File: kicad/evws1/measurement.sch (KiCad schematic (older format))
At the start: 0 parts

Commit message: ...
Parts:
- added C40: 100n, Project:c-1206-hand-soldering, symbol Device:C_Small
- added C41, C42, C43, C44: 10n, Project:c-1206-hand-soldering, symbol Device:C_Small
- added C45, C46: 1n, Project:c-1206-hand-soldering, symbol Device:C_Small
- added R59, R60: 100R, Project:r-0805-hand-soldering, symbol Device:R
- added R81, R82: 820R, Project:r-0805-hand-soldering, symbol Device:R
- added R83, R84: 1K2, Project:r-0805-hand-soldering, symbol Device:R
- added R85, R87: 18K, Project:r-0805-hand-soldering, symbol Device:R
- added R86, R88: 0R, Project:r-0805-hand-soldering, symbol Device:R
- added R89, R90: 15K, Project:r-0805-hand-soldering, symbol Device:R
- added RV2, RV3: 100R, Project:trimmer-tht-3296, symbol Device:R_POT_TRIM
- added RV4, RV5, RV6, RV7: 1K, Project:trimmer-tht-3296, symbol Device:R_POT_TRIM
- added U13: LM224, Project:soic-16_hand-soldering, symbol _project:LM224
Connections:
- net AD-I1: now also C45.2, RV6.2
- net AD-I2: now also C46.2, RV7.2
- net AD-V1: now also C43.2, R89.1, U13.7
- net AD-V2: now also C44.2, R90.1, U13.14
- net I1: now also RV6.1
- net I2: now also RV7.1
- net V1P: now also R59.2
- net V2P: now also R60.2
- net VREF-2V5: now also RV4.3, RV5.3
- new net: C41.1, R59.1, R81.2, U13.2 (-)
- new net: C41.2, R83.2, RV2.1, RV2.2, U13.1
- new net: C43.1, R83.1, R86.1, R89.2, U13.6 (-)
- new net: R81.1, RV2.3
- new net: R85.2, RV4.1, RV4.2
- new net: R85.1, R86.2
- new net: C42.1, R60.1, R82.2, U13.9 (-)
- new net: C42.2, R84.2, RV3.1, RV3.2, U13.8
- new net: C44.1, R84.1, R88.1, R90.2, U13.13 (-)
- new net: R82.1, RV3.3
- new net: R87.2, RV5.1, RV5.2
- new net: R87.1, R88.2
- new net +12V: C40.2, U13.4 (V+)
- new net -12V: U13.11 (V-)
- new net GND: C40.1, C45.1, C46.1, RV6.3, RV7.3, U13.10 (+), U13.12 (+), U13.3 (+), U13.5 (+)
- no-connect marks 0 -> 1

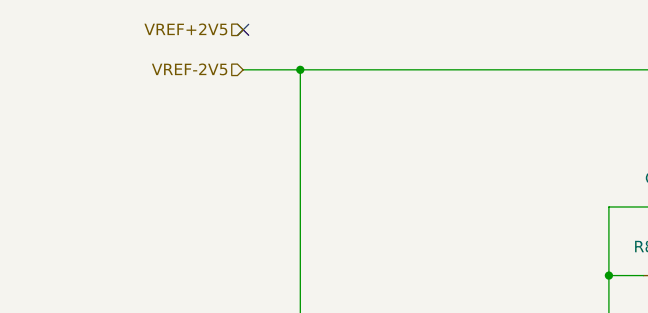
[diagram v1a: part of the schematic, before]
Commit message: Schematic completed, no DRC errors left
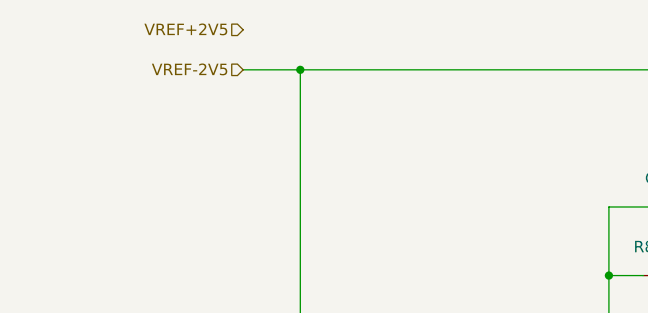
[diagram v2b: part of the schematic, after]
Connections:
- no-connect marks 1 -> 0
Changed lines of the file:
@@
 Text HLabel 2050 925  0    50   Input ~ 0
 VREF+2V5
-NoConn ~ 2050 925
 $Comp
 L power:GND #PWR?

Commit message: schematic finished
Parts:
- added D18, D19: BAT54S, Project:sot-23_hand-soldering, symbol _project:BAT54S
- added J21, J22: header, Project:idc-header-1x03-p2.54mm-vertical, symbol Connector_Generic:Conn_01x03
- added R6, R7: 1K, Project:r-0805-hand-soldering, symbol Device:R
- R83, R84: value 1K2 -> 3K3
- R85, R87: value 18K -> 15K
- R86, R88: value 0R -> 4K7
- R89, R90: value 15K -> 10K
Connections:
- net AD-I1: now also J21.3 (Pin_3)
- net AD-I2: now also J22.3 (Pin_3)
- net AD-V1: now also D18.3, J21.2 (Pin_2), R6.1; no longer C43.2, R89.1, U13.7
- net AD-V2: now also D19.3, J22.2 (Pin_2), R7.1; no longer C44.2, R90.1, U13.14
- net GND: now also D18.1, D19.1, J21.1 (Pin_1), J22.1 (Pin_1)
- new net: C43.2, R6.2, R89.1, U13.7
- new net: C44.2, R7.2, R90.1, U13.14
- new net +5V: D18.2, D19.2
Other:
- moved on the sheet: C42, C44, C45, C46, R60, R82, R83, R84, R87, R88, R90, RV3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

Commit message: ...
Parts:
- removed U13: LM224, Project:soic-16_hand-soldering, symbol _project:LM224
- added C52, C53, C54: 100n, Project:c-1206-hand-soldering, symbol Device:C_Small
- added U13, U14: LM258, Project:soic-8_hand-soldering, symbol _project:LM258
- R59, R6, R60, R7, R81, R82, R83, R84, R85, R86, R87, R88, R89, R90: footprint Project:r-0805-hand-soldering -> Project:r-1206-hand-soldering
- renumbered RV4 to RV3, RV3 to RV4
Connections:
- net +12V: now also C52.2, U13.4 (V-), U14.4 (V-)
- net -12V: now also C53.1, C54.1, U13.8 (V+), U14.8 (V+)
- net GND: now also C52.1, C53.2, C54.2, U13.3 (+), U13.5 (+), U14.3 (+), U14.5 (+)
- net at C41.1, R59.1, R81.2: now also U13.2 (-)
- net at C41.2, R83.2, RV2.1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: now also U13.1
- net at C43.1, R83.1, R86.1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: now also U13.6 (-)
- net at C43.2, R6.2, R89.1: now also U13.7
- net at C44.2, R7.2, R90.1: now also U14.7
- net at C42.1, R60.1, R82.2: now also U14.2 (-)
- net at C42.2, R84.2, RV4.1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: now also U14.1
- net at C44.1, R84.1, R88.1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: now also U14.6 (-)
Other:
- moved on the sheet: C40

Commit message: ...
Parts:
- removed C40, C53: 100n, Project:c-1206-hand-soldering, symbol Device:C_Small
- removed J21, J22: header, Project:idc-header-1x03-p2.54mm-vertical, symbol Connector_Generic:Conn_01x03
- removed U13, U14: LM258, Project:soic-8_hand-soldering, symbol _project:LM258
- added U13: LM224, Project:soic-14_hand-soldering, symbol _project:LM224
- renumbered R90 to R4
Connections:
- net +12V: now also U13.4 (V+)
- net -12V: now also U13.11 (V-)
- net GND: now also U13.10 (+), U13.12 (+), U13.3 (+), U13.5 (+)
- net at C41.1, R59.1, R81.2: now also U13.9 (-)
- net at C41.2, R83.2, RV2.1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: now also U13.8
- net at C43.1, R83.1, R86.1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: now also U13.13 (-)
- net at C43.2, R6.2, R89.1: now also U13.14
- net at C42.2, R84.2, RV4.1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: now also U13.7
- net at C42.1, R60.1, R82.2: now also U13.6 (-)
- net at C44.1, R4.2, R84.1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: now also U13.2 (-)
- net at C44.2, R4.1, R7.2: now also U13.1

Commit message: schematic finished, placement finished
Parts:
- added C27, C55: 1pF, Project:c-1206-hand-soldering, symbol Device:C_Small
- added C56, C57, C59, C60: 100n, Project:c-1206-hand-soldering, symbol Device:C_Small
- added C58: 1u, Project:c-1206-hand-soldering, symbol Device:C_Small
- added D21: BAT54S, Project:sot-23_hand-soldering, symbol _project:BAT54S
- added R107, R117: 1K, Project:r-1206-hand-soldering, symbol Device:R
- added R108, R113, R114, R115: 10K, Project:r-1206-hand-soldering, symbol Device:R
- added R109, R110, R111, R112: 0R, Project:r-1206-hand-soldering, symbol Device:R
- added R116: 470K, Project:r-1206-hand-soldering, symbol Device:R
- added U14: LM258, Project:soic-8_hand-soldering, symbol _project:LM258
- added U15: AD633AR, Project:soic-8_hand-soldering, symbol _project:AD633AR
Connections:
- net +12V: now also C57.1, C59.1, U14.8 (V+), U15.6 (+VS)
- net +5V: now also D21.2
- net -12V: now also C56.1, C60.1, U14.4 (V-), U15.3 (-VS)
- net GND: now also C27.1, C55.1, C56.2, C57.2, C59.2, C60.2, D21.1, R109.2, R113.1, U14.3 (+), U14.5 (+)
- net I1: now also R112.2
- net VREF+2V5: now also R111.2
- net at C41.2, R83.2, RV2.1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: now also R107.2
- new net: R111.1, U15.1 (Y1)
- new net: C55.2, R112.1, U15.2 (Y2)
- new net: R113.2, U15.4 (Z)
- new net: R114.2, U15.5 (W)
- new net: R109.1, U15.7 (X1)
- new net: C27.2, R110.1, U15.8 (X2)
- new net: R107.1, R108.2, U14.6 (-)
- new net: R108.1, R110.2, U14.7
- new net: C58.2, R116.1, R117.2, U14.1
- new net: C58.1, R114.1, R115.1, R116.2, U14.2 (-)
- new net AOUT: R115.2
- new net E1: D21.3, R117.1
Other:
- moved on the sheet: C41, C42, C43, C44, C45, C46, C52, C54, D18, D19, R4, R59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

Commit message: ...
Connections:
- net GND: now also RV6.1; no longer RV6.3
- net I1: now also RV6.3; no longer RV6.1
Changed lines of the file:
@@
 F 3 "~" H 5700 4000 50  0001 C CNN
 	1    5700 4000
-	1    0    0    -1
+	1    0    0    1
 $EndComp
 $Comp

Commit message: V1.0 Design finished
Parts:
- renumbered D19 to D3, D21 to D4
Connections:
- net P1: now reaches R114.2, U15.5 (W)
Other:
- moved on the sheet: C58, C59, C60, D4, R114, R115, R116, R117, U14A, U14C
